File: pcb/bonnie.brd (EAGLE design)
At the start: 27 x 24.8 mm, 9 parts

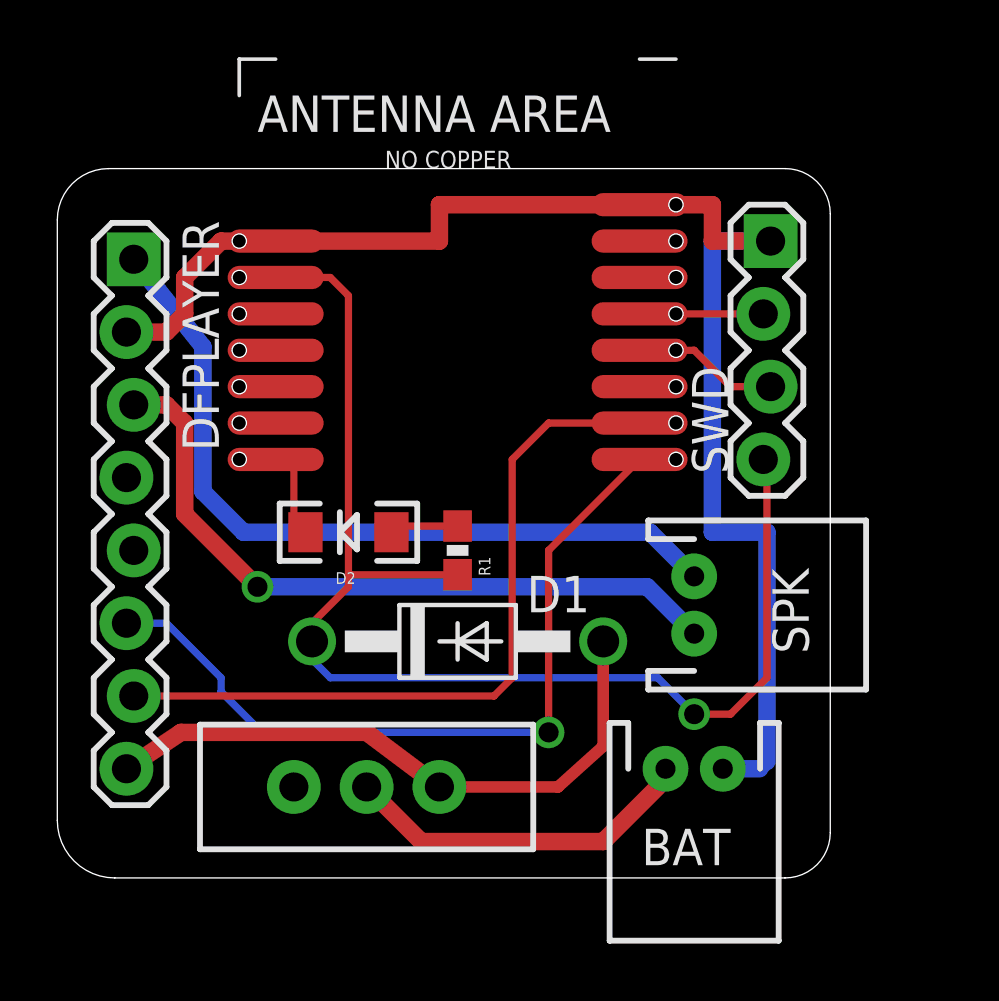
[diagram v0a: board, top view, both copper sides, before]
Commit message: add charging mechanism, replace diode with a regulator
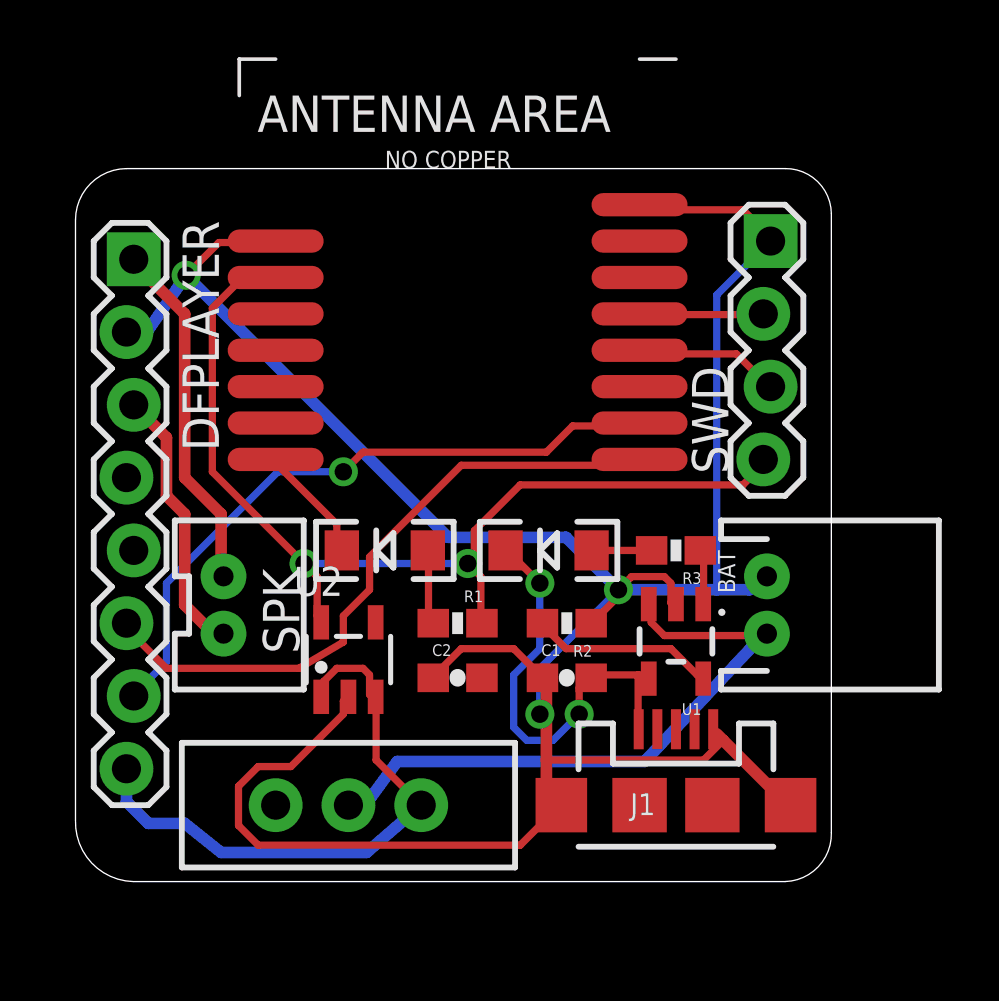
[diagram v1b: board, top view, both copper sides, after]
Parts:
- removed D1: 1N4004, diode:DO41-10
- added C1, C2: 4.7uF, SparkFun-Passives:0603-CAP
- added D3: RED, SparkFun-LED:LED-1206
- added J1: USB-MICROB, SparkFun-Connectors:USB-MICROB
- added R2: 2k, SparkFun-Resistors:0603-RES
- added R3: 4k7, SparkFun-Resistors:0603-RES
- added U1: MCP73831, SparkFun-PowerIC:SOT23-5
- added U2: RT9013-XXXB, v-reg-new:SOT23-5
- D2: value RED -> BLUE
- SPK: device SparkFun-Connectors:JST-2-PTH -> SparkFun-Connectors:JST-2-PTH-VERT
- moved SPK 15.9 mm to (31.1, 38.1)
- moved BAT 6.25 mm to (49.5, 38.1), turned to 270 degrees
- moved R1 2.54 mm to (38.7, 37.5), turned to 180 degrees
- moved D2 1.42 mm to (36.2, 40.0)
- moved S1 0.90 mm to (34.9, 31.1)
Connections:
- new net N$4: R3.1, U1.1
- new net N$5: D3.A, R3.2
- new net VBAT: BAT.2, S1.2, U1.3
- new net VBUS: C1.2, D3.C, J1.VBUS, U1.4
- net GND: now also C1.1, C2.1, J1.GND, J1.MT1, J1.MT2, R2.1, U1.2, U2.2
- net N$1: now also R2.2, U1.5; no longer BAT.2, S1.2
- net VDD: now also U2.5; no longer D1.C
- net VIN: now also U2.1, U2.3; no longer D1.A
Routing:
- net GND: track 50.8 -> 98.9 mm, vias 0 -> 3
- net VBAT: track 0.00 -> 22.3 mm
- net VBUS: track 0.00 -> 15.4 mm, vias 0 -> 2
- net SPK1: track 24.7 -> 9.49 mm, vias 1 -> 0
- net SPK2: track 27.3 -> 12.4 mm
- net VDD: track 44.7 -> 35.7 mm, vias 1 -> 2
- net N$1: track 12.4 -> 6.42 mm
- net RX: track 27.4 -> 22.8 mm, vias 1 -> 0
- net TX: track 26.1 -> 23.3 mm, vias 0 -> 1
- net N$5: track 0.00 -> 2.10 mm
- net N$4: track 0.00 -> 1.99 mm
- net VIN: track 21.9 -> 20.5 mm
- net N$3: track 3.58 -> 4.22 mm
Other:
- board size 27 x 24.8 mm -> 26.4 x 24.9 mm
- board text removed: "SPK"
